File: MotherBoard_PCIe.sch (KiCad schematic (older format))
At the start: 40 parts, among them J1 Conn_01x02, J10 Bus_mechaken_PCIexpress_x16_1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, J11 Conn_01x03, J12 Conn_01x03, J2 Conn_01x02, J3 Conn_01x07, J4 Conn_01x07, J5 Bus_mechaken_PCIexpress_x16_1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, J6 Bus_mechaken_PCIexpress_x16_1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, J7 Bus_mechaken_PCIexpress_x16_1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, J8 Bus_mechaken_PCIexpress_x16_1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, J9 Bus_mechaken_PCIexpress_x16_1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, U1 L7812

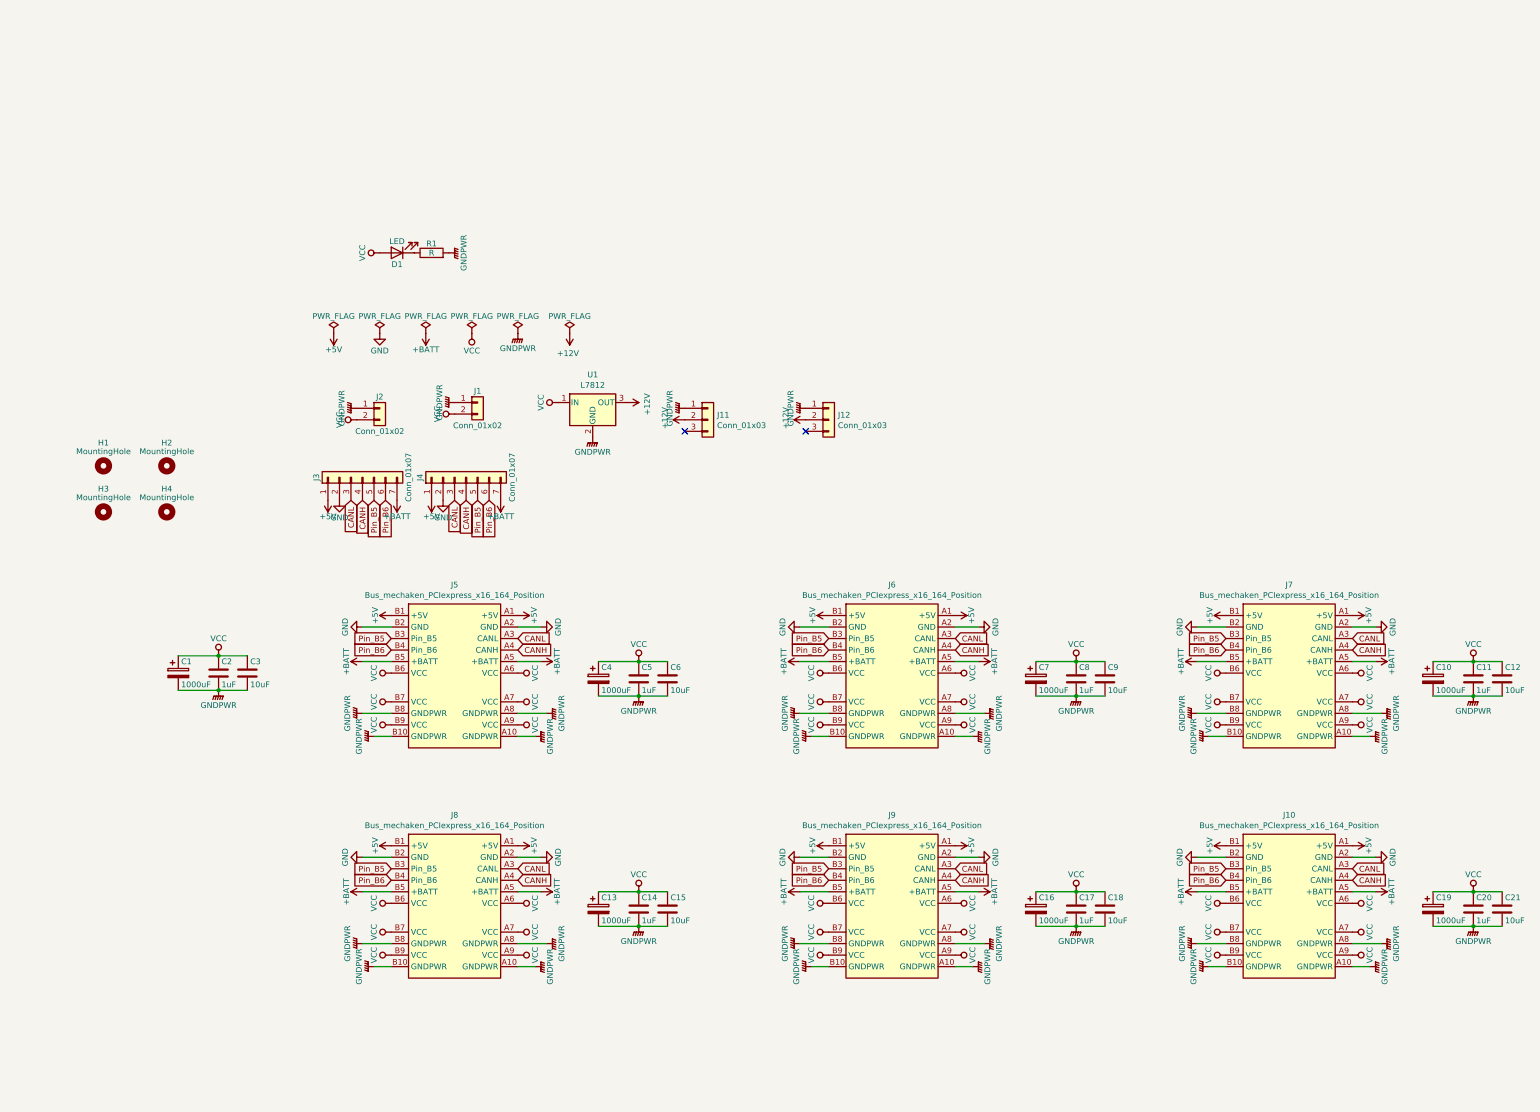
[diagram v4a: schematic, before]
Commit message: add
通電確認用LEDとファンコネクタを1つ追加
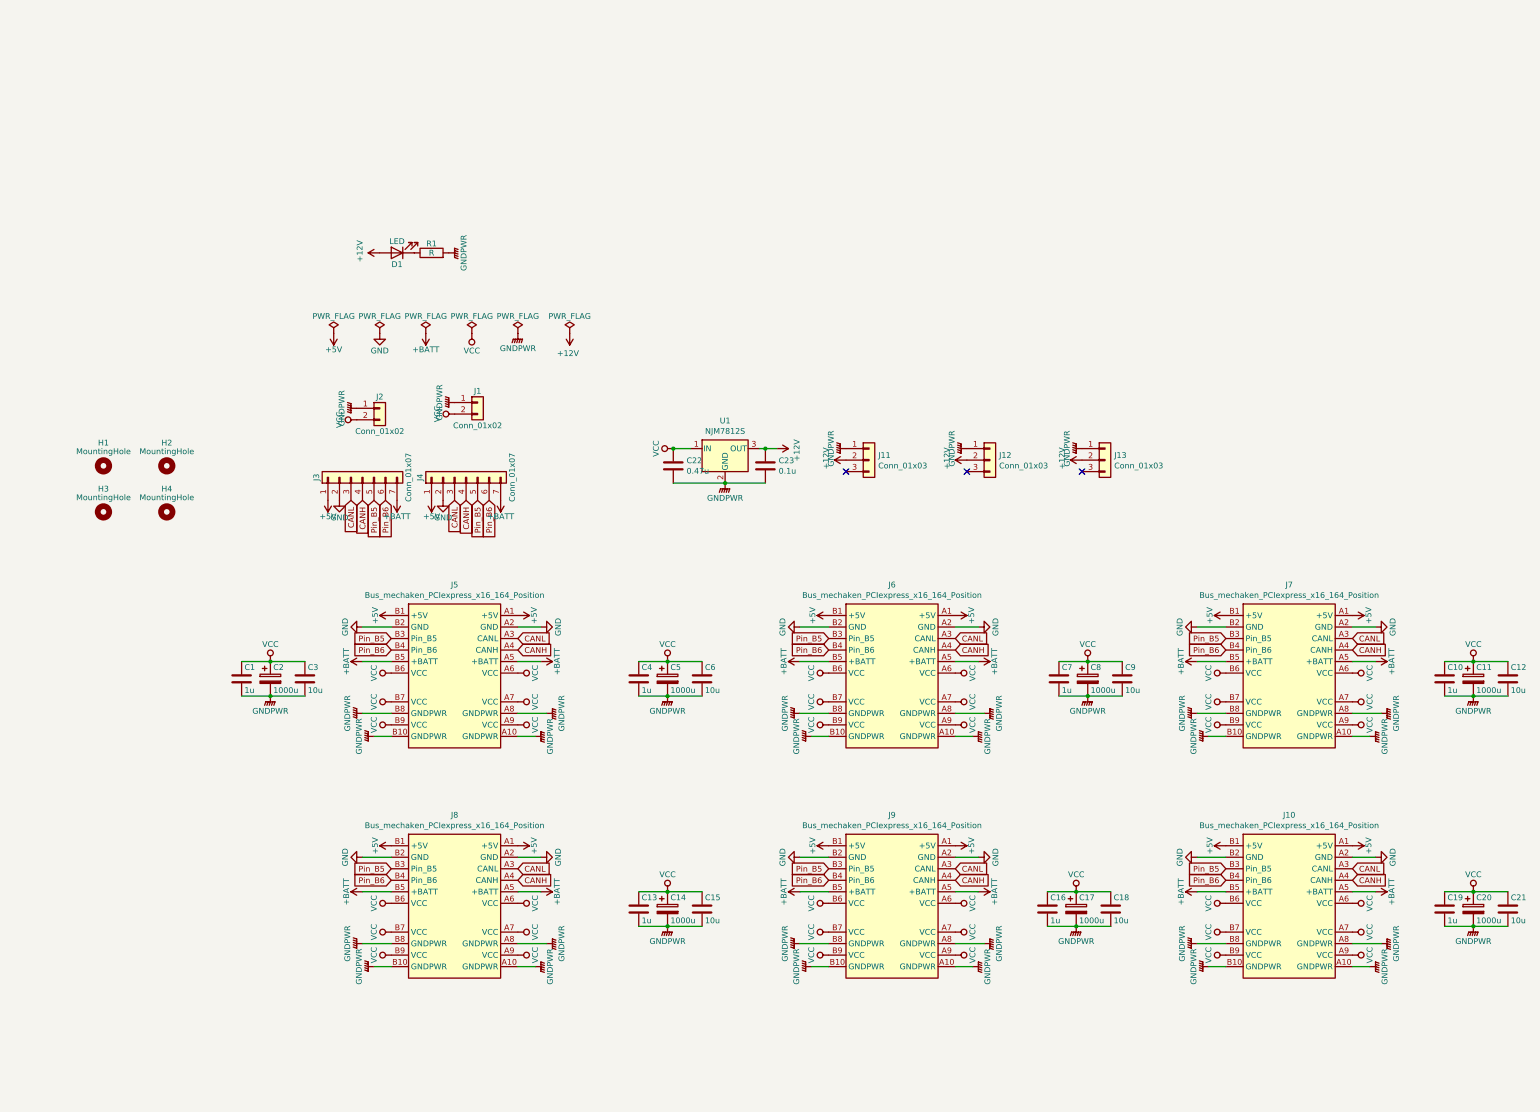
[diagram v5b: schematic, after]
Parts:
- removed C1, C10, C13, C16, C4, C7: 1000uF, Capacitor_THT:CP_Radial_D12.5mm_P5.00mm, symbol Device:CP
- removed C11, C14, C17, C2, C5, C8: 1uF, Capacitor_SMD:C_0805_2012Metric, symbol Device:C
- added C1, C10, C13, C16, C4, C7: 1u, Capacitor_SMD:C_0805_2012Metric, symbol Device:C
- added C11, C14, C17, C2, C5, C8: 1000u, Capacitor_THT:CP_Radial_D12.5mm_P5.00mm, symbol Device:CP
- added C22: 0.47u, Capacitor_SMD:C_0805_2012Metric, symbol Device:C
- added C23: 0.1u, Capacitor_SMD:C_0805_2012Metric, symbol Device:C
- added J13: Conn_01x03, Connector:FanPinHeader_1x03_P2.54mm_Vertical, symbol Connector_Generic:Conn_01x03
- C12, C15, C18, C21, C3, C6, C9: value 10uF -> 10u
- C19: renamed from C20; value 1uF -> 1u
- C20: renamed from C19; value 1000uF -> 1000u
- R1: footprint Resistor_THT:R_Axial_DIN0207_L6.3mm_D2.5mm_P10.16mm_Horizontal -> Resistor_SMD:R_0603_1608Metric_Pad1.05x0.95mm_HandSolder
- U1: value L7812 -> NJM7812S; footprint Package_TO_SOT_THT:TO-220-3_Vertical -> Package_TO_SOT_SMD:TO-252-2
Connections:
- net +12V: now also D1.2 (A), C23.1, J13.2 (Pin_2)
- net GNDPWR: now also C1.2, C10.2, C11.2, C13.2, C14.2, C16.2, C17.2, C2.2, C22.2, C23.2, C4.2, C5.2, C7.2, C8.2, J13.1 (Pin_1)
- net VCC: now also C1.1, C10.1, C11.1, C13.1, C14.1, C16.1, C17.1, C2.1, C22.1, C4.1, C5.1, C7.1, C8.1; no longer D1.2 (A)
- no-connect marks 2 -> 3
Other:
- moved on the sheet: C19, C20, C21

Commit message: clean
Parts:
- C22: value 0.47u -> 0.33u
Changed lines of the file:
@@
 P 6250 4500
 F 0 "C22" H 6365 4546 50  0000 L CNN
-F 1 "0.47u" H 6365 4455 50  0000 L CNN
+F 1 "0.33u" H 6365 4455 50  0000 L CNN
 F 2 "Capacitor_SMD:C_0805_2012Metric" H 6288 4350 50  0001 C CNN
 F 3 "~" H 6250 4500 50  0001 C CNN

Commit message: add
step file
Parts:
- J1: value Conn_01x02 -> XT60-M
- J2: value Conn_01x02 -> XT60-F
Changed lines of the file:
@@
 P 3700 4000
 F 0 "J2" H 3700 4100 50  0000 C CNN
-F 1 "Conn_01x02" H 3700 3800 50  0000 C CNN
+F 1 "XT60-F" H 3700 3800 50  0000 C CNN
 F 2 "Connector_AMASS:AMASS_XT60-F_1x02_P7.20mm_Vertical" H 3700 4000 50  0001 C CNN
 F 3 "~" H 3700 4000 50  0001 C CNN
@@
 P 4550 3950
 F 0 "J1" H 4550 4050 50  0000 C CNN
-F 1 "Conn_01x02" H 4550 3750 50  0000 C CNN
+F 1 "XT60-M" H 4550 3750 50  0000 C CNN
 F 2 "Connector_AMASS:AMASS_XT60-M_1x02_P7.20mm_Vertical" H 4550 3950 50  0001 C CNN
 F 3 "~" H 4550 3950 50  0001 C CNN

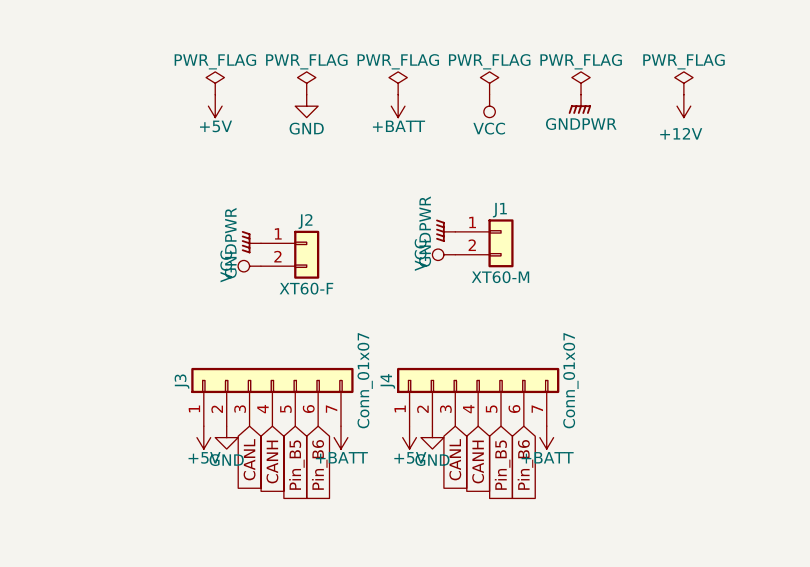
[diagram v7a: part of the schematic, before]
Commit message: change
シルク印刷の修正（githubのリンク等）
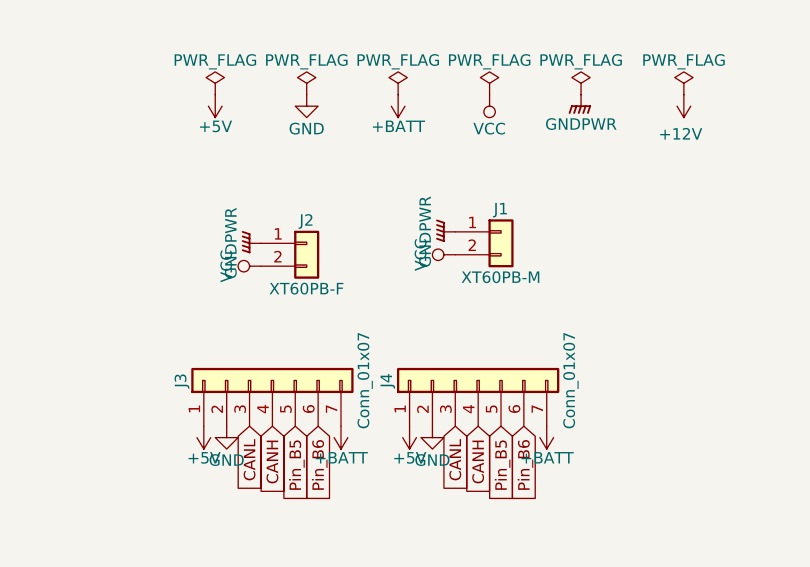
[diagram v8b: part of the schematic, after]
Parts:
- J1: value XT60-M -> XT60PB-M
- J2: value XT60-F -> XT60PB-F
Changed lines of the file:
@@
 P 3700 4000
 F 0 "J2" H 3700 4100 50  0000 C CNN
-F 1 "XT60-F" H 3700 3800 50  0000 C CNN
+F 1 "XT60PB-F" H 3700 3800 50  0000 C CNN
 F 2 "Connector_AMASS:AMASS_XT60-F_1x02_P7.20mm_Vertical" H 3700 4000 50  0001 C CNN
 F 3 "~" H 3700 4000 50  0001 C CNN
@@
 P 4550 3950
 F 0 "J1" H 4550 4050 50  0000 C CNN
-F 1 "XT60-M" H 4550 3750 50  0000 C CNN
+F 1 "XT60PB-M" H 4550 3750 50  0000 C CNN
 F 2 "Connector_AMASS:AMASS_XT60-M_1x02_P7.20mm_Vertical" H 4550 3950 50  0001 C CNN
 F 3 "~" H 4550 3950 50  0001 C CNN
